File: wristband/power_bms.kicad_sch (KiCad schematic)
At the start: 21 parts, among them J1 USB4125-GF-A, Q1 AO3401A, Q2 FS8205A, U1 DW01A, U2 MCP73831T-2ACI/OT

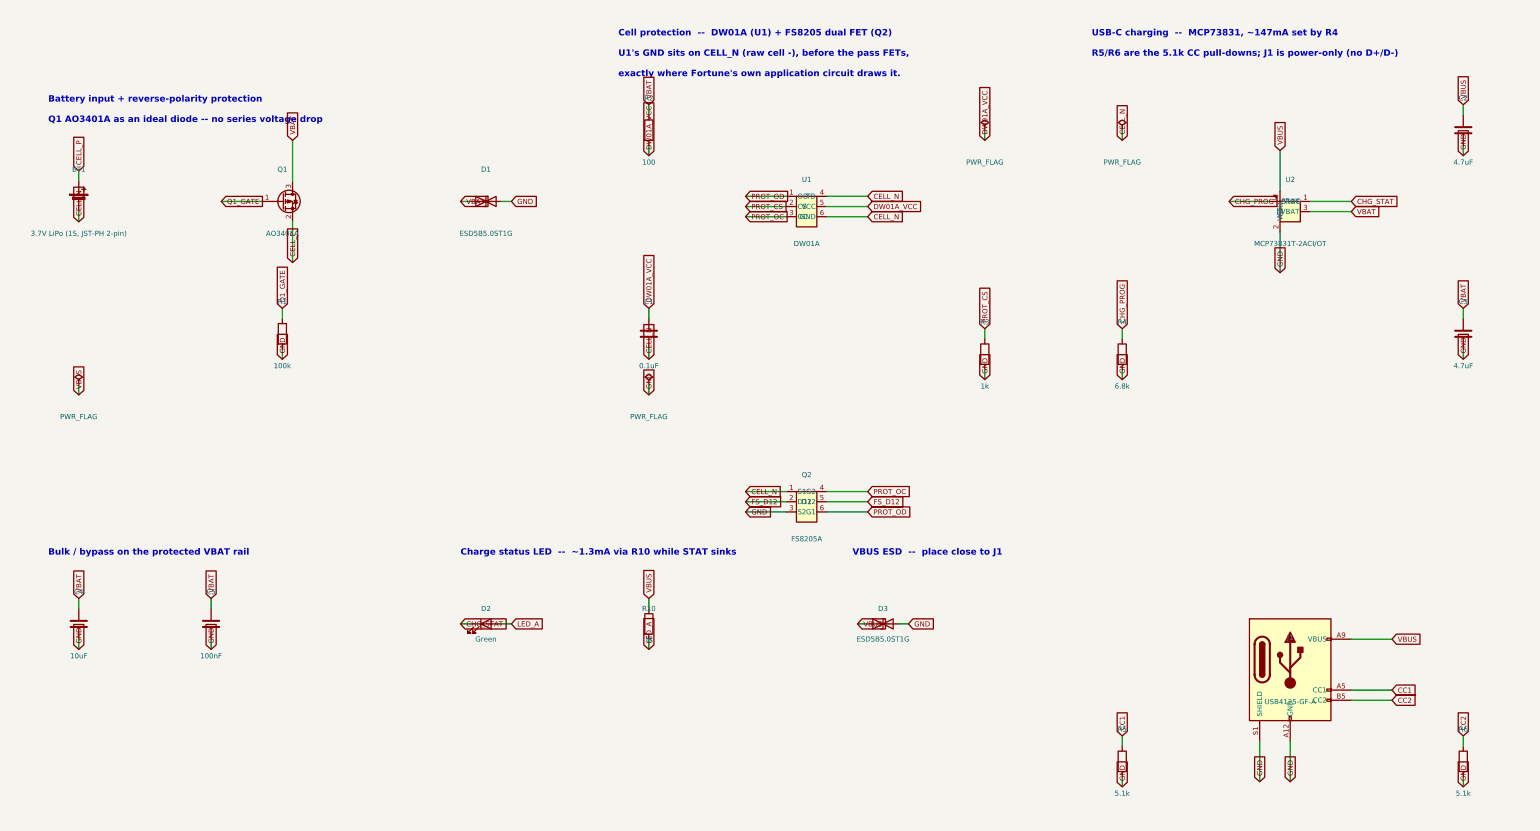
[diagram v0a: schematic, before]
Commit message: Convert global labels to power symbols; import footprints to PCB
Continues the ground cleanup from 0263e7f across the rest of the wristband
sheets: global labels replaced with explicit power symbols and wired
junctions, so connections are drawn rather than implied by name.

                     wires      labels      junctions   symbols
  power_bms          61 -> 83   61 -> 51    0 -> 3      25 -> 36
  programming_debug   7 ->  8    7 ->  4    0 -> 1       1 ->  3
  radio_mcu          71 -> 79   64 -> 42    7 -> 17     18 -> 32
  regulation          7 ->  7    7 ->  4    0 -> 0       3 ->  6

The added symbols are all power ports, so the BOM is untouched: still 47
components, 76 nets, 42 no-connects, 35 analyzer findings with 1 error --
identical before and after. The one error is the known DW01A false
positive (U1.6 GND sits on CELL_N by design, per the reference circuit).

Also ran Update PCB from Schematic on the wristband: 0 -> 46 footprints.
Nothing routed yet, no zones, board outline unchanged.

Co-Authored-By: Claude Opus 5 (1M context) <noreply@anthropic.com>
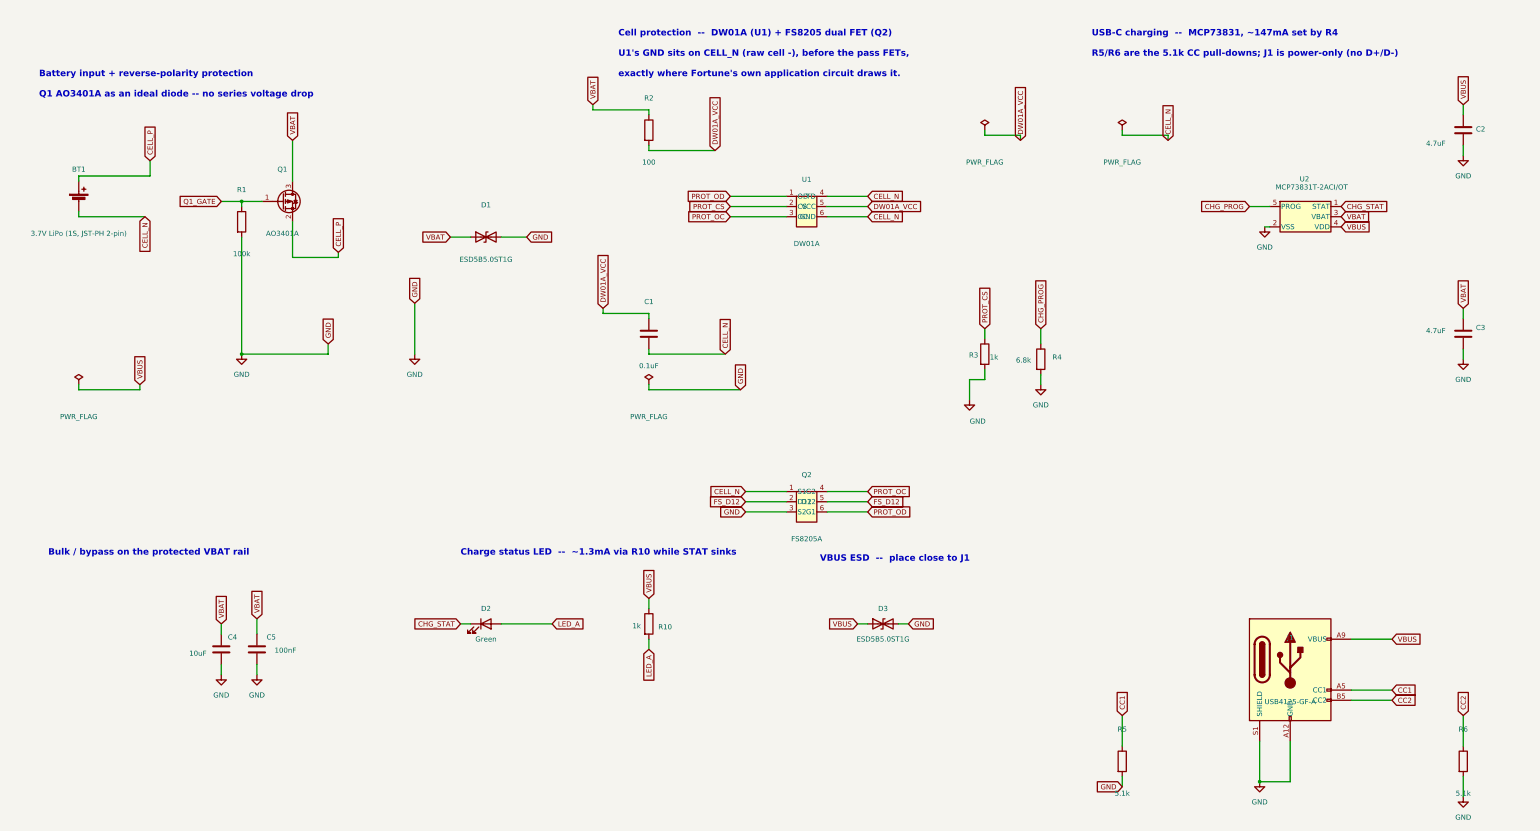
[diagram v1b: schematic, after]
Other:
- moved on the sheet: C4, C5, D1, R1, R4, U2

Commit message: Migrate wristband to DWM3001C; swap LDO to TPS7A02; fix ERC
Replace the NINA-B400 + DWM3000 pair with a single Qorvo DWM3001C, then
replace the MCP1700 LDO with a nanopower TI TPS7A0233. Wristband ERC goes
from 1 error / 13 warnings to 0 errors / 1 warning.

DWM3001C (U4), verified against Qorvo DS Rev B May 2022:
- Integrates DW3110 UWB + nRF52833 BLE MCU + LIS2DH12 + UWB antenna +
  Bluetooth chip antenna + 38.4MHz crystal. Its nRF52833 is now the host,
  so U3 (NINA-B400) is deleted.
- The DW3110<->nRF52833 SPI is internal, so the board-level UWB SPI bus,
  IRQ/RSTn/WAKEUP, the GPIO5/6 SPI-mode straps (R7/R8), the IRQ pulldown
  (R9) and the external LFXO (Y1/C14/C15) are all gone. C8-C10 too.
- AE1 (PRO-IS-237) removed: the module carries both antennas, so
  antenna.kicad_sch is documentation-only and places nothing.
- SWD moved for the first time: SWD_CLK=2, SWD_DIO=3, RESET=47 (P0.18),
  SWO=28 (P1.00). Battery sense moved to P0.02 = AIN0. Both P1.00=SWO and
  P0.02=AIN0 confirmed in nRF52833 PS v1.7 p825-826.
- Symbol + DWM3001C_PLACEHOLDER footprint are wristband-only, in libs/.
  The footprint has TWO unresolved dimensions (side pitch back-derives to
  1.06375mm; bottom pad row width undimensioned and apparently off-centre).
  VERIFY BEFORE FAB.

TPS7A0233PDBVR (U5), verified against TI SBVS277C:
- Iq 1.6uA typ / 4uA max -> 25nA typ / 46nA max; it was the largest single
  standby draw, bigger than the DWM3001C's own 850nA sleep. Board standby
  ~4.3uA -> ~2.7uA. Accuracy +/-1.5% vs +/-2.5%.
- Not a drop-in: SOT-23-5 1=IN 2=GND 3=EN 4=NC 5=OUT. EN ties to VBAT
  because TPS7A02 is disabled when EN floats and the MCU on this rail
  cannot enable its own supply.
- C12 1uF -> 2.2uF for the 0.5uF effective-capacitance stability floor.
- Symbol is self-contained: KiCad ships no TPS7A02, and every TPS7A05
  sibling is extends-based, which kicad-cli cannot load.

ERC fixes:
- Real bug: regulation.kicad_sch had no labels at all, so U5's input and
  C11 sat on an iso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
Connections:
- net GND: now also J1.SH (SHIELD); no longer J1.S1 (SHIELD)
- net LED_A: no longer names the net of D2.2 (A), R10.2
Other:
- moved on the sheet: C1, C2, C3, C4, C5, D1, D2, Q2, R10, R2, R3, R4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
